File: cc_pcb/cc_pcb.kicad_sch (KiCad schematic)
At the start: 74 parts, among them J1 Conn_02x05_Odd_Even, J10 AC-DC Converter, J11 2.8in SPI TFT Touch Display, J2 Wi-Fi Module, J3 Controller (40Pin->SPI), J5 4x4 Keypad, J7 PS_Modules, J8 PS_Designed, J9 DC-DC Converter, SW1 SW_Push, U1 STM32F091RCTx, U3 LD1117S33TR_SOT223, U4 TPS56325x

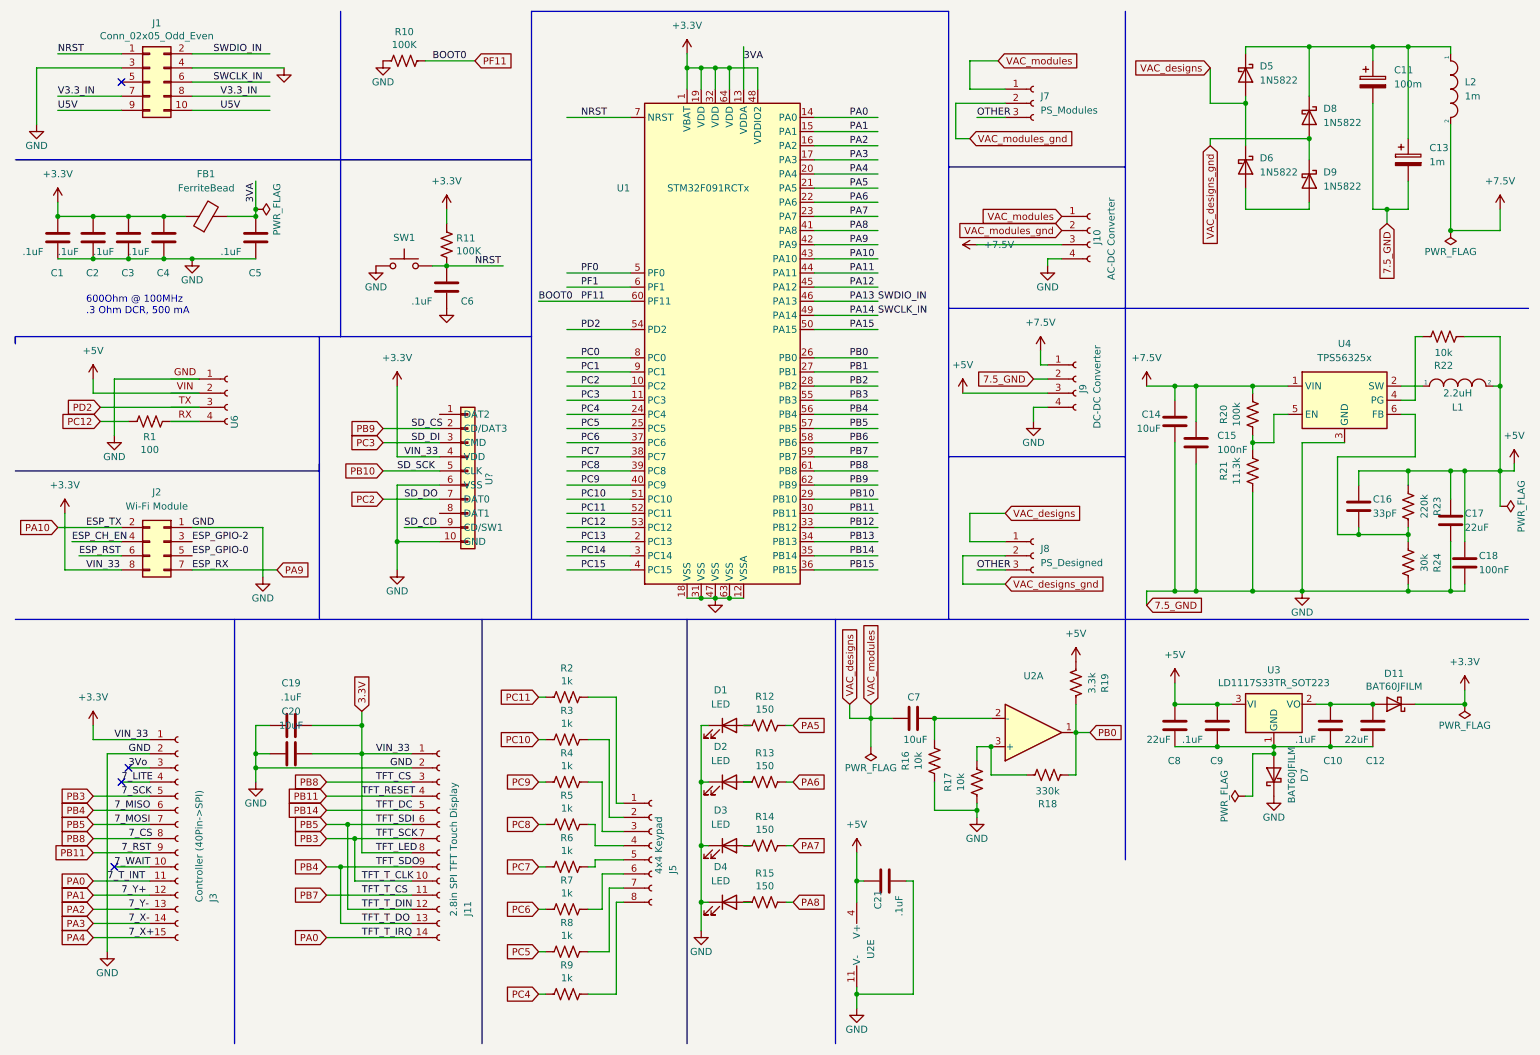
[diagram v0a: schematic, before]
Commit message: updated symbols to include pin names to get rid of ERC warnings
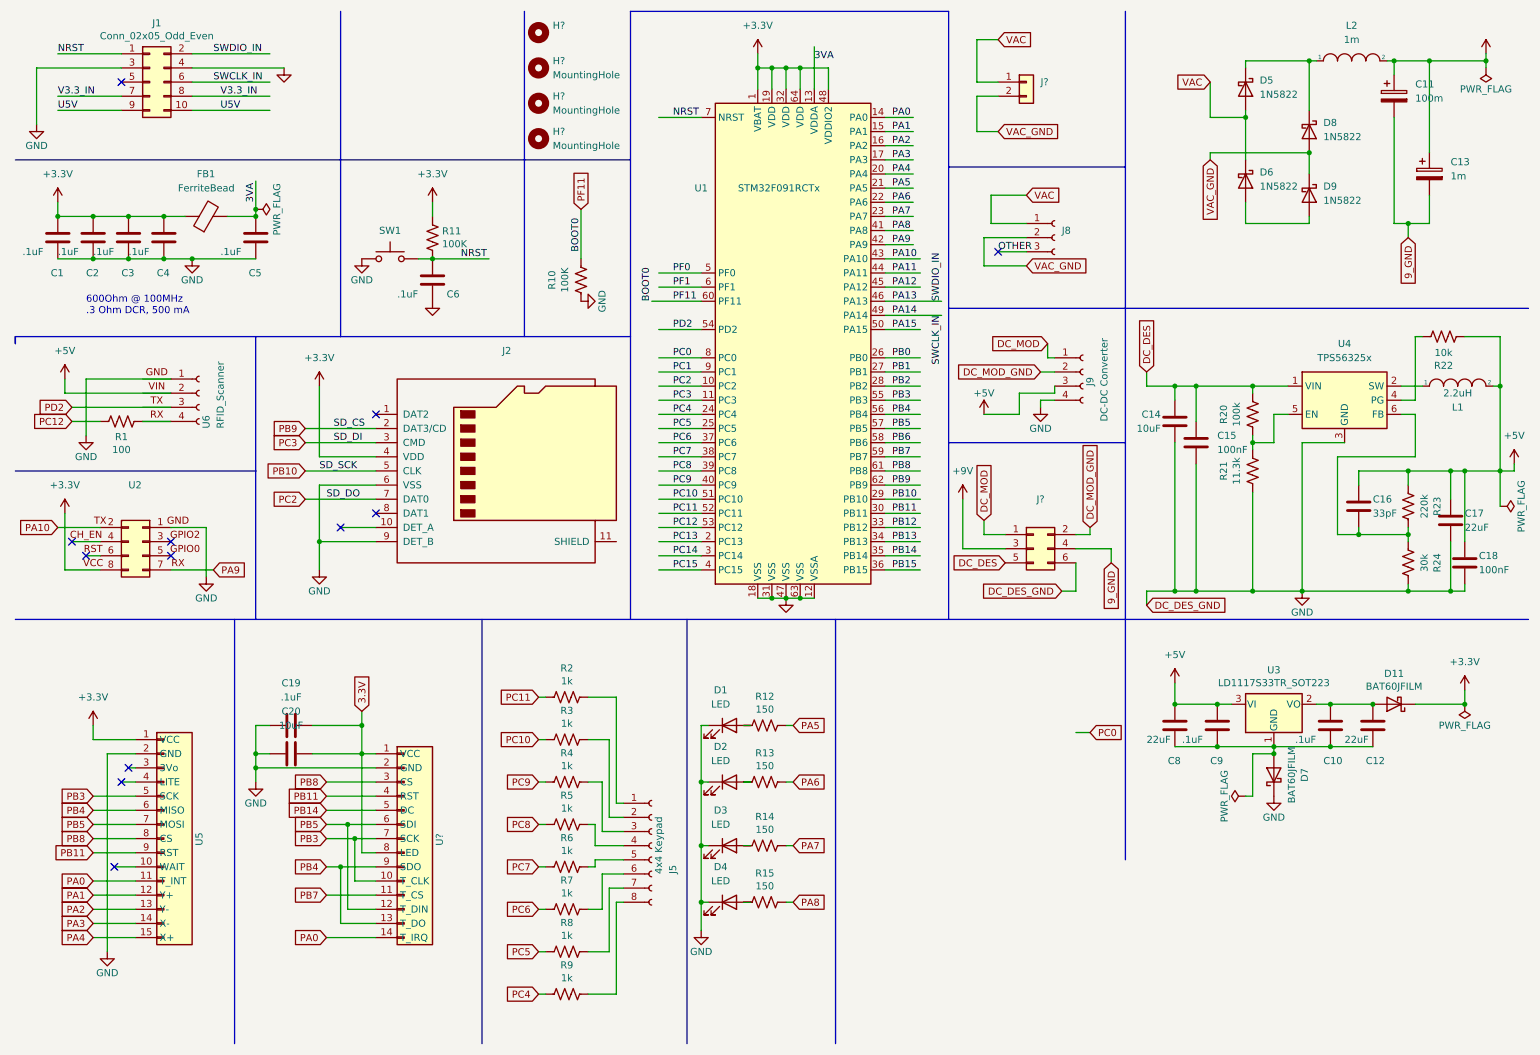
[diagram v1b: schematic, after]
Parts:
- removed C21: .1uF, Capacitor_SMD:C_0805_2012Metric_Pad1.18x1.45mm_HandSolder, symbol Device:C
- removed C7: 10uF, Capacitor_SMD:C_0805_2012Metric_Pad1.18x1.45mm_HandSolder, symbol Device:C
- removed J10: AC-DC Converter, imported_footprints:7.5Vdc-5Vdc_buck_converter, symbol Connector:Conn_01x04_Female
- removed J11: 2.8in SPI TFT Touch Display, imported_footprints:tft_2.8in_touch_display, symbol Connector:Conn_01x14_Female
- removed J2: Wi-Fi Module, imported_footprints:XCVR_ESP8266-01_ESP-01, symbol Connector_Generic:Conn_02x04_Odd_Even
- removed J3: Controller (40Pin->SPI), symbol Connector:Conn_01x15_Female
- removed J7: PS_Modules, imported_footprints:barrel_jack_adapter, symbol Connector:Conn_01x03_Female
- removed R16, R17: 10k, Resistor_SMD:R_0805_2012Metric_Pad1.20x1.40mm_HandSolder, symbol Device:R_US
- removed R18: 330k, Resistor_SMD:R_0805_2012Metric_Pad1.20x1.40mm_HandSolder, symbol Device:R_US
- removed R19: 3.3k, Resistor_SMD:R_0805_2012Metric_Pad1.20x1.40mm_HandSolder, symbol Device:R_US
- removed U2: (no value), symbol Amplifier_Operational:LM324
- removed U?: (no value), symbol created_schematics:wurth_SD
- added H? (x3): MountingHole, symbol Mechanical:MountingHole
- added H?: (no value), symbol Mechanical:MountingHole
- added J2: (no value), symbol Connector:Micro_SD_Card_Det_Hirose_DM3AT
- added J?: (no value), symbol Connector_Generic:Conn_02x03_Odd_Even
- added J?: (no value), symbol Connector_Generic:Conn_01x02
- added U2: (no value), symbol created_schematics:ESP8266
- added U5: (no value), symbol created_schematics:7in_display_controller
- added U?: (no value), symbol created_schematics:TFT_2.8IN_DISPLAY
- C19, C20, C5: footprint (none) -> Capacitor_SMD:C_0805_2012Metric_Pad1.18x1.45mm_HandSolder
- FB1: footprint (none) -> Resistor_SMD:R_0805_2012Metric_Pad1.20x1.40mm_HandSolder
- J8: value PS_Designed -> (none)
- U6: value (none) -> RFID_Scanner; footprint (none) -> imported_footprints:RFID_Reader_PCB
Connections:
- net +3V3: now also J2.4 (VDD), U2.8, U5.1 (VCC); no longer C19.2, C20.2, U1.30 (PB11)
- net GND: now also J2.6 (VSS), J2.9 (DET_B), J?.6 (Pin_6), U2.1, U5.2 (GND), U?.2 (GND); no longer C11.2, C13.2, J9.2 (Pin_2), U1.14 (PA0)
- net PA1: now also U5.12 (Y+)
- net PA10: now also U2.2
- net PA2: now also U5.13 (Y-)
- net PA3: now also U5.14 (X-)
- net PA4: now also U5.15 (X+)
- net PA9: now also U2.7
- net PB10: now also J2.5 (CLK)
- net PB14: now also U?.5 (DC)
- net PB3: now also U5.5 (SCK), U?.10 (T_CLK), U?.7 (SCK)
- net PB4: now also U5.6 (MISO), U?.13 (T_DO), U?.9 (SDO)
- net PB5: now also U5.7 (MOSI), U?.12 (T_DIN), U?.6 (SDI)
- net PB7: now also U?.11 (T_CS)
- net PB8: now also U5.8 (CS), U?.3 (CS)
- net PB9: now also J2.2 (DAT3/CD)
- net PC2: now also J2.7 (DAT0)
- net PC3: now also J2.3 (CMD)
- net at D5.1 (K), D8.1 (K), L2.1: no longer C11.1, C13.1
- net +7.5V renamed DC_DES
- net DC_DES: now also J?.5 (Pin_5); no longer J9.1 (Pin_1), L2.2
- net VAC_designs renamed VAC
- net VAC: now also J?.1 (Pin_1)
- net VAC_designs_gnd renamed VAC_GND
- net VAC_GND: now also J?.2 (Pin_2)
- new net +9V: C11.1, C13.1, J?.3 (Pin_3), L2.2
- new net 3.3V: C19.2, C20.2, U?.1 (VCC), U?.8 (LED)
- new net 9_GND: C11.2, C13.2, J?.4 (Pin_4)
- new net DC_MOD: J9.1 (Pin_1), J?.1 (Pin_1)
- new net DC_MOD_GND: J9.2 (Pin_2), J?.2 (Pin_2)
- new net PA0: U1.14 (PA0), U5.11 (T_INT), U?.14 (T_IRQ)
- new net PB11: U1.30 (PB11), U5.9 (RST), U?.4 (RST)
- no-connect marks 4 -> 12
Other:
- moved on the sheet: C11, C13, C6, D5, D6, D8, D9, J8, J9, R1, R10, R11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

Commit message: passed ERC and footprints assigned
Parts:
- added C15: .1uF, Capacitor_SMD:C_0805_2012Metric_Pad1.18x1.45mm_HandSolder, symbol Device:C
- added D1: (no value), symbol Device:LED
- added D10, D11: 1N5822, imported_footprints:DIO_1N5822, symbol Device:D_Schottky
- added D2, D3: LED, symbol Device:LED
- added R2: 100K, Resistor_SMD:R_0805_2012Metric_Pad1.20x1.40mm_HandSolder, symbol Device:R_US
- added R21, R22, R3, R4: (no value), Resistor_SMD:R_0805_2012Metric_Pad1.20x1.40mm_HandSolder, symbol Device:R_US
- added R25, R27: (no value), symbol Device:R_US
- added U5: (no value), symbol 74xx:74HC14
- added U9: (no value), symbol Isolator:4N28
- gave numbers to parts that had none: 7
- renumbered C9 to C10, C10 to C11, C14 to C13, C15 to C14, C11 to C17, C13 to C18, C17 to C19, C18 to C20, C19 to C6, C20 to C7, C6 to C8, C8 to C9, D5 to D12, D6 to D13, D8 to D14, D9 to D15, D1 to D4, D2 to D5, D3 to D6, D4 to D7, D7 to D8, D11 to D9, J5 to J3, J8 to J6, J9 to J7, L2 to L1, L1 to L2, R6 to R10, R7 to R11, R8 to R12, R9 to R13, R10 to R14, R12 to R15, R13 to R16, R14 to R17, R15 to R18, R20 to R19, R21 to R20, R22 to R26, R11 to R5, R2 to R6, R3 to R7, R4 to R8, R5 to R9, U2 to U1, U5 to U2, U6 to U3, U1 to U6, U3 to U7, U4 to U8
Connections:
- net +3V3: now also C15.1, R27.1, R4.1, U5.14 (VCC), U5.3, U5.5
- net +5V: now also R3.1
- net +9V: now also R2.1
- net GND: now also J2.11 (SHIELD), C15.2, D1.1 (K), D2.1 (K), D3.1 (K), R25.1, U5.11, U5.13, U5.7 (GND), U5.9, U9.4
- net PC0: now also U5.2
- net VAC: now also D10.2 (A)
- net VAC_GND: now also D11.2 (A), U9.2
- new net: R27.2, U5.1, U9.5
- new net: D2.2 (A), R3.2
- new net: R22.1, U9.1
- new net: R21.1, R22.2
- new net: D1.2 (A), R2.2
- new net: D3.2 (A), R4.2
- new net: D10.1 (K), D11.1 (K), R21.2
- new net: R25.2, U9.6
- no-connect marks 12 -> 17
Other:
- moved on the sheet: C10, C11, C12, C9, D4, D5, D6, D7, D8, D9, J5, R15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

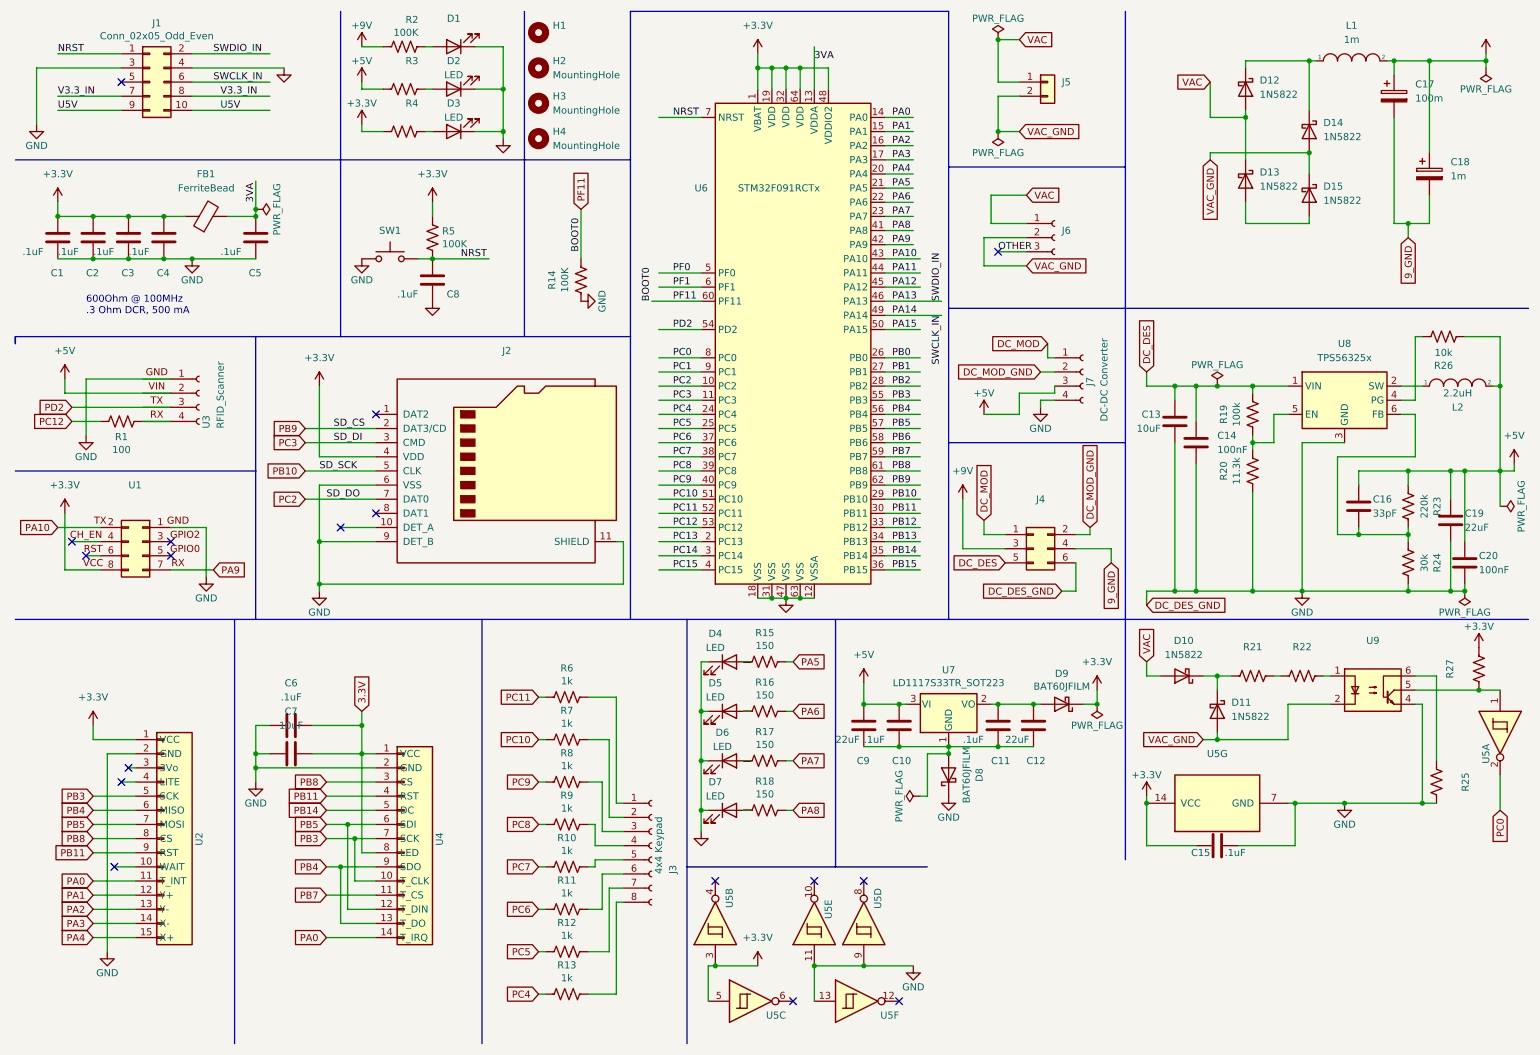
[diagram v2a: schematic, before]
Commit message: initial PCB components, traces laid out with DRC passed
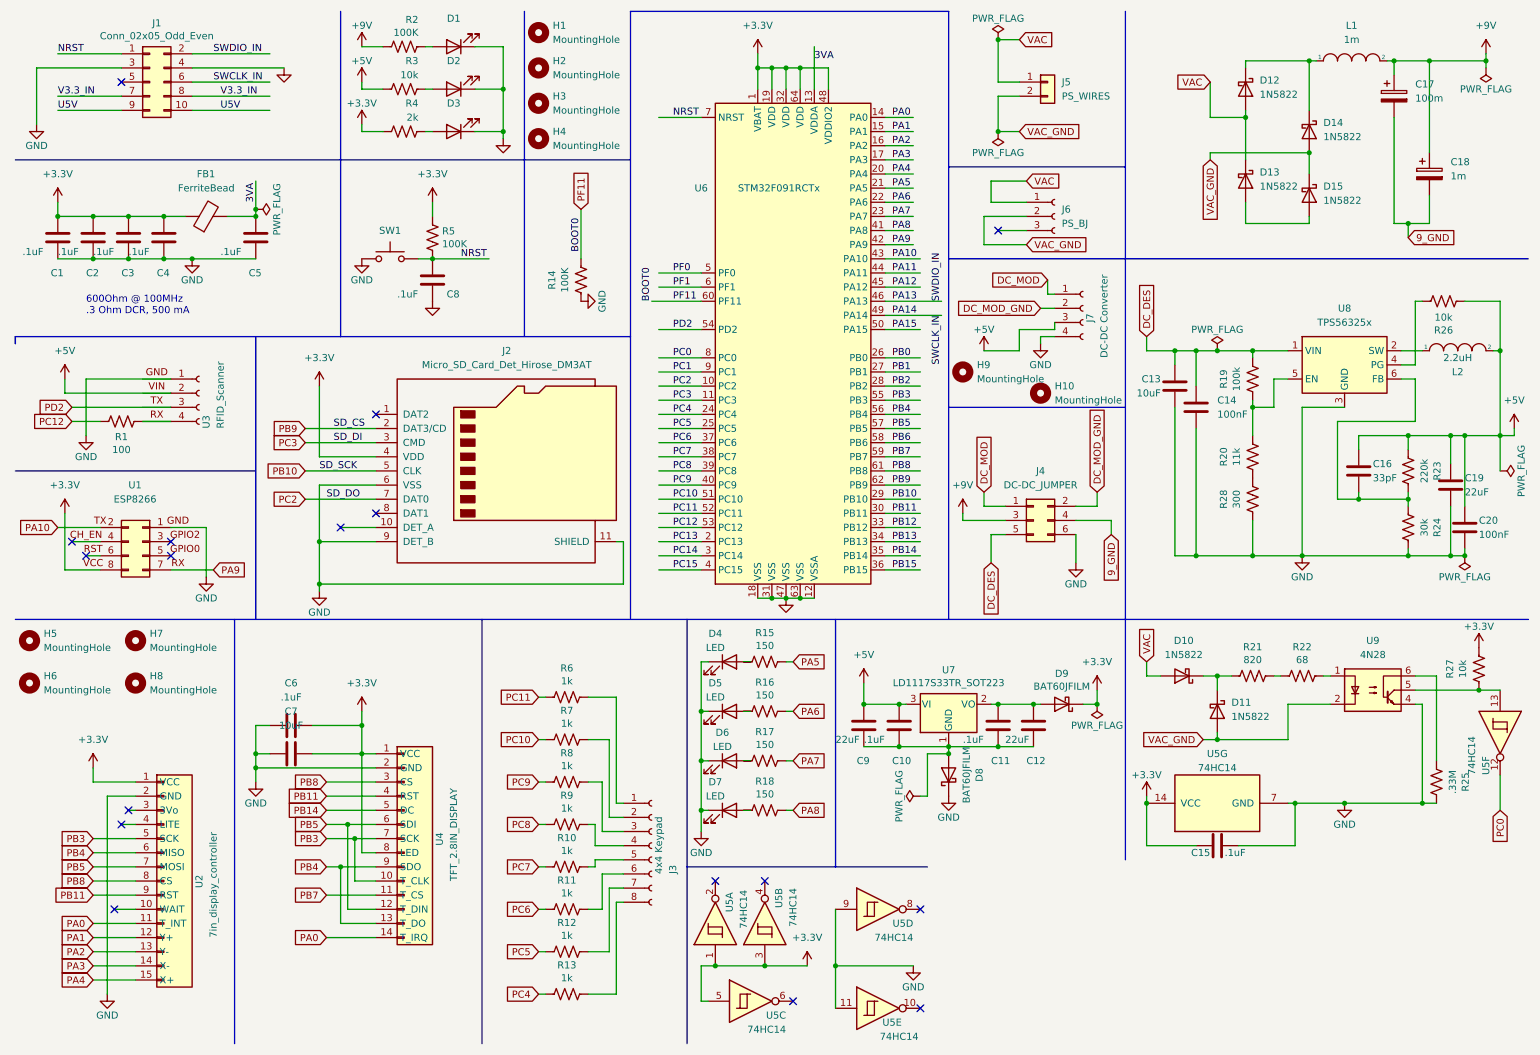
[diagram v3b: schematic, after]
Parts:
- added H10, H6, H7, H8: MountingHole, MountingHole:MountingHole_2.2mm_M2_ISO7380, symbol Mechanical:MountingHole
- added H5, H9: MountingHole, symbol Mechanical:MountingHole
- added R28: 300, Resistor_SMD:R_0805_2012Metric_Pad1.20x1.40mm_HandSolder, symbol Device:R_US
- D1: footprint (none) -> LED_SMD:LED_0805_2012Metric_Pad1.15x1.40mm_HandSolder
- D2, D3: value LED -> (none); footprint (none) -> LED_SMD:LED_0805_2012Metric_Pad1.15x1.40mm_HandSolder
- H1: value (none) -> MountingHole
- H3, H4: footprint (none) -> MountingHole:MountingHole_8.4mm_M8
- J2: value (none) -> Micro_SD_Card_Det_Hirose_DM3AT; footprint (none) -> Connector_Card:microSD_HC_Hirose_DM3AT-SF-PEJM5
- J4: value (none) -> DC-DC_JUMPER; footprint (none) -> Connector_PinSocket_1.27mm:PinSocket_2x03_P1.27mm_Vertical
- J5: value (none) -> PS_WIRES; footprint (none) -> imported_footprints:PS_2_Wire
- J6: value (none) -> PS_BJ
- R20: value 11.3k -> 11k
- R21: value (none) -> 820
- R22: value (none) -> 68
- R25: value (none) -> .33M; footprint (none) -> Resistor_SMD:R_0805_2012Metric_Pad1.20x1.40mm_HandSolder
- R27: value (none) -> 10k; footprint (none) -> Resistor_SMD:R_0805_2012Metric_Pad1.20x1.40mm_HandSolder
- R3: value (none) -> 10k
- R4: value (none) -> 2k
- U1: value (none) -> ESP8266; footprint (none) -> imported_footprints:XCVR_ESP8266-01_ESP-01
- U2: value (none) -> 7in_display_controller
- U4: value (none) -> TFT_2.8IN_DISPLAY; footprint (none) -> imported_footprints:tft_2.8in_touch_display
- U5: value (none) -> 74HC14; footprint (none) -> imported_footprints:SN74HC14N
- U8: footprint imported_footprints:TPS56325x -> (none)
- U9: value (none) -> 4N28; footprint (none) -> Package_DIP:DIP-6_W7.62mm
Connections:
- net 3.3V is gone; now on net +3V3: C6.2, C7.2, U4.1 (VCC), U4.8 (LED)
- net +3V3: now also U5.1
- net GND: now also R28.2; no longer R20.2, U5.13
- net PC0: now also U5.12; no longer U5.2
- net at R27.2, U9.5: now also U5.13; no longer U5.1
- net OTHER: no longer names the net of J6.3 (Pin_3)
- new net: R20.2, R28.1
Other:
- moved on the sheet: C13, C14, C16, C19, C20, J4, J6, J7, L2, R19, R20, R23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
